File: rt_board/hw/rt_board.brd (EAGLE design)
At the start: 63.8 x 73.7 mm, 67 parts, among them IC1 MCP170333MB, IC2/L1 TLE4935L, IC3/L2 TLE4935L, IC4/R1 TLE4935L, IC5/R2 TLE4935L, Q1 8MHz, SW1 B3U-1000PM-B, SW2 B3U-1000PM-B, U1 DRV8801PWP, U2 DRV8801PWP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

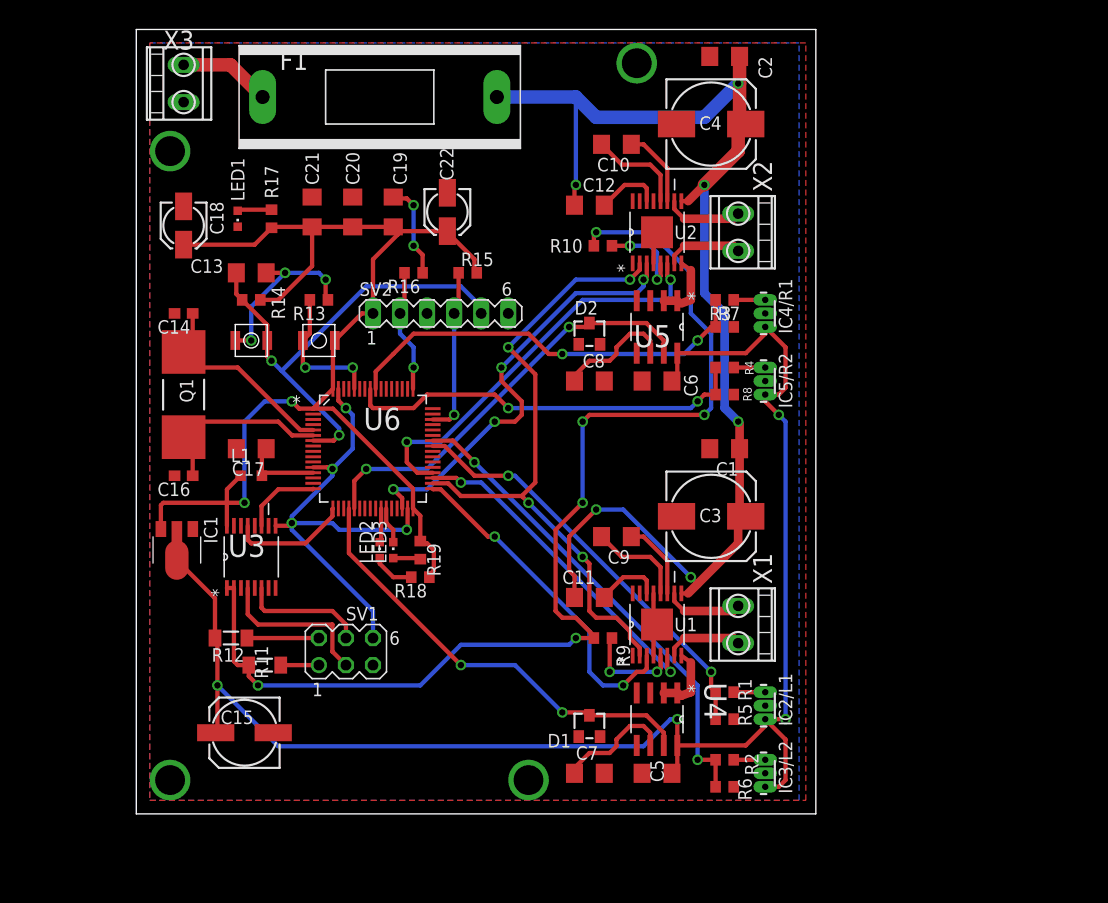
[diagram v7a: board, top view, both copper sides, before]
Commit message: added 1000uF to +12V input for extra decoupling
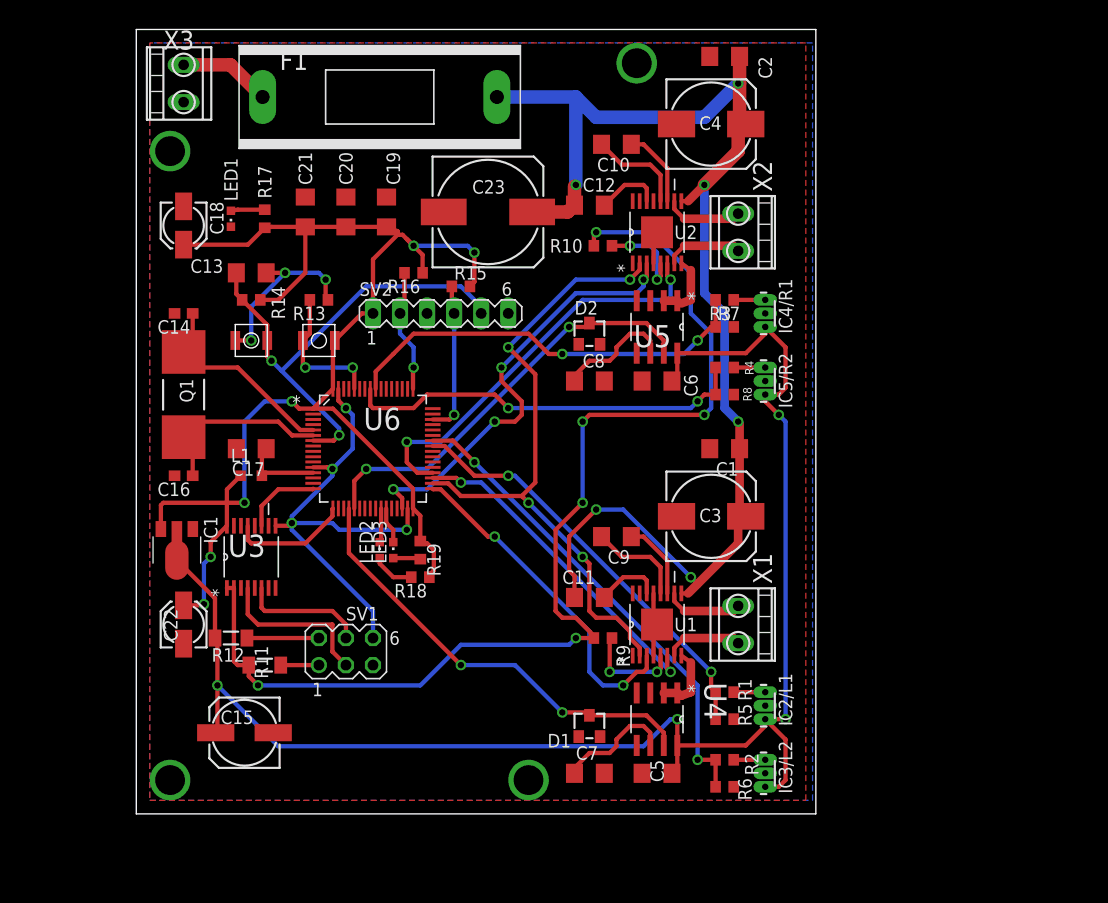
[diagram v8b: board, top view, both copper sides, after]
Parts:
- added C23: 1000uF, rcl:153CLV-1014
- moved C22 46.0 mm to (15.2, 24.1), turned to 90 degrees
- moved R15 1.42 mm to (41.3, 55.9)
- moved LED1 0.64 mm to (19.7, 62.2)
- moved R17 0.64 mm to (22.9, 62.2)
- moved C19 0.63 mm to (34.3, 62.9)
- moved C20 0.63 mm to (30.5, 62.9)
- moved C21 0.63 mm to (26.7, 62.9)
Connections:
- net +12V: now also C23.+
- net 0V: now also C23.-
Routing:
- net +5V: track 113.7 -> 125.0 mm, vias 2 -> 6
- net 0V: track 81.1 -> 76.0 mm, vias 13 -> 11
- net +12V: track 117.8 -> 122.1 mm
- net N$9: track 15.7 -> 14.9 mm
